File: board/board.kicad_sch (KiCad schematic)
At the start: 22 parts, among them J1 UART, J2 008_USB, J3 DebugEdge_02x05, J4 SPI_2x3, J5 ADC_2x3, J6 I2C_2x2, J7 SPI_2x3, J8 I2C_2x2, J9 UART_2x2

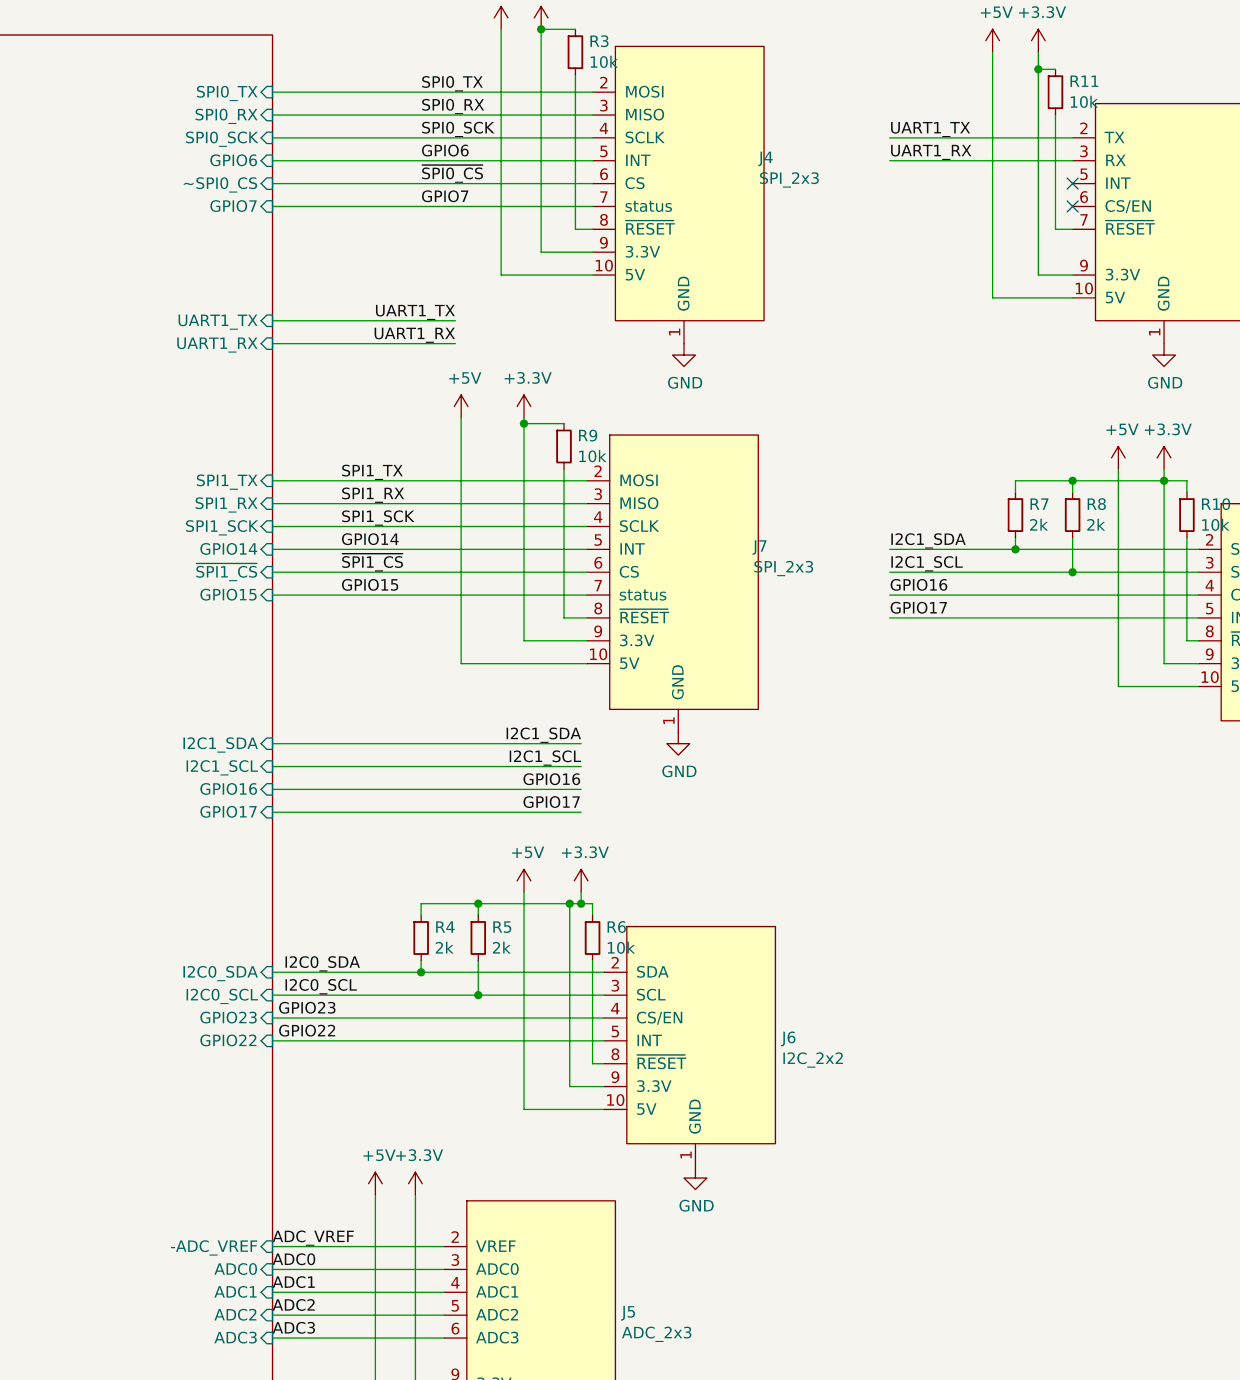
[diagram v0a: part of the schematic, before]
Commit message: changed top I2C connector to be a UNIO connector for a mac address chip
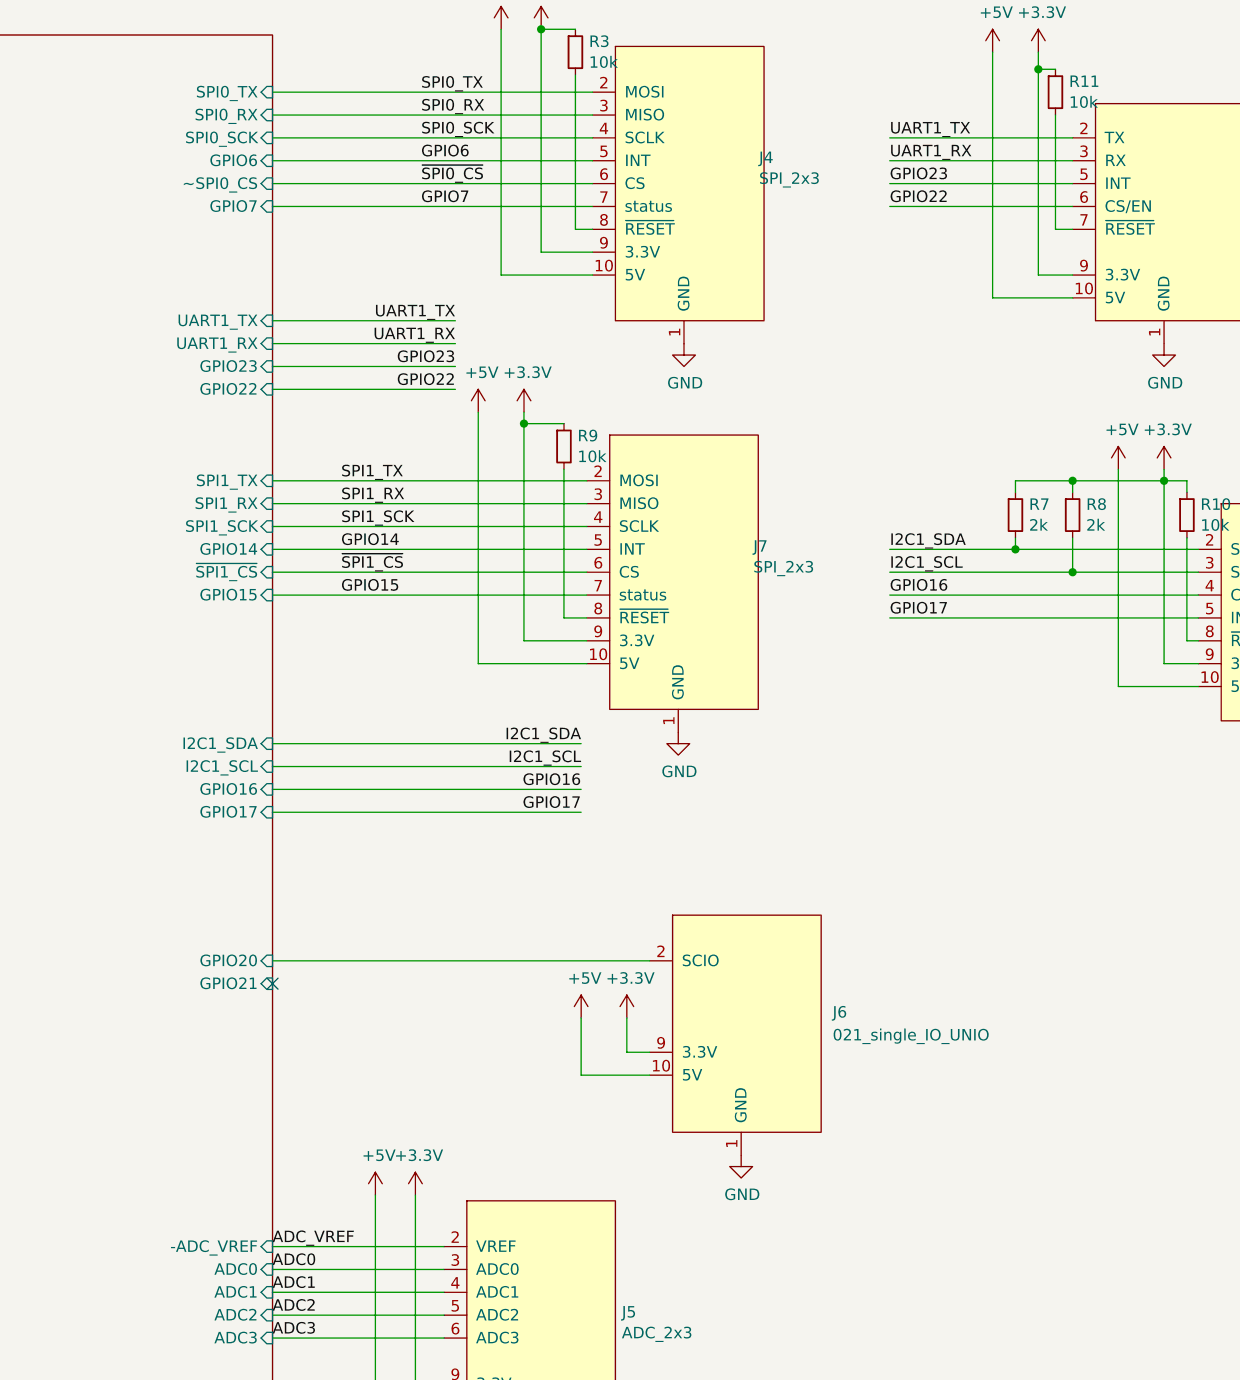
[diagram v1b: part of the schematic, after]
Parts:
- removed J6: I2C_2x2, on_edge:on_edge_2x05_up_host, symbol put_on_edge:001_I2C
- removed R4, R5: 2k, Resistor_SMD:R_0603_1608Metric, symbol Device:R_Small
- removed R6: 10k, Resistor_SMD:R_0603_1608Metric, symbol Device:R_Small
- added J6: 021_single_IO_UNIO, on_edge:on_edge_2x05_up_host, symbol put_on_edge:021_single_IO_UNIO
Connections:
- net +3V3: now also J6.9 (3.3V)
- net +5V: now also J6.10 (5V)
- net GND: now also J6.1 (GND)
- net GPIO22: now also J9.6 (CS/EN)
- net GPIO23: now also J9.5 (INT)
- new net rp2040/GPIO20: J6.2 (SCIO)
- no-connect marks 12 -> 11
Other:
- sheet rp2040 ports: added GPIO20, GPIO21; removed I2C0_SCL, I2C0_SDA

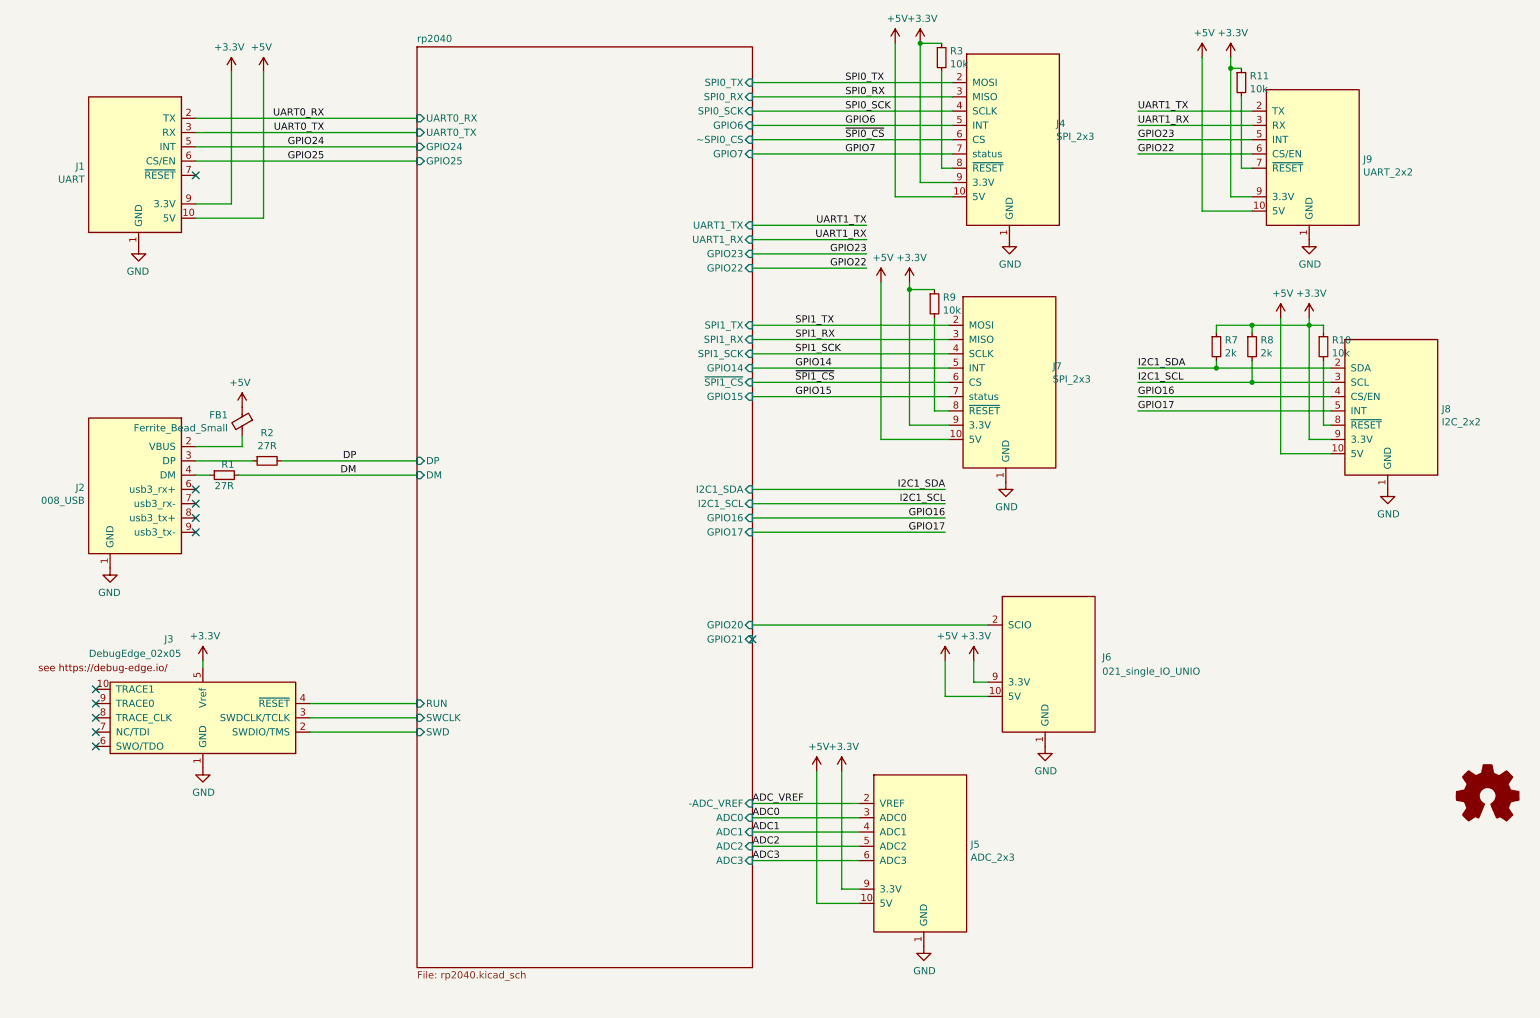
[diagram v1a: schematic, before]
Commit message: changed power symbols in subsheets
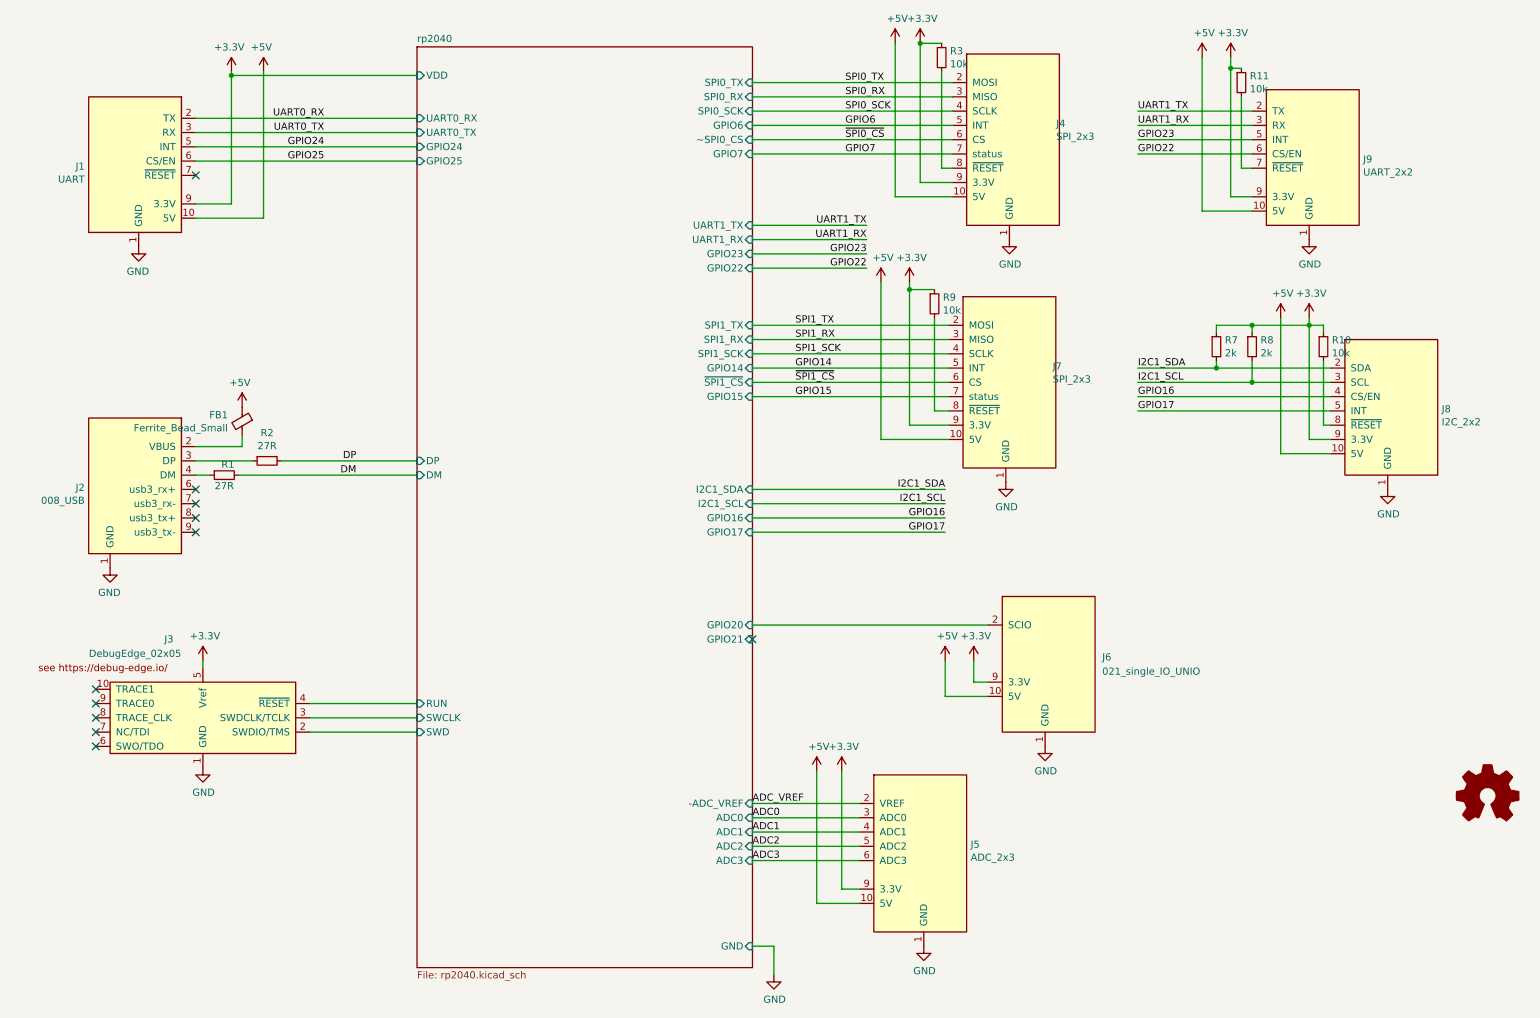
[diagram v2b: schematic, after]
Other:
- sheet rp2040 ports: added GND, VDD; removed none
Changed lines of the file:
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@@
   (junction (at 241.3 69.85) (diameter 0) (color 0 0 0 0)
+  )
+  (junction (at 49.53 25.4) (diameter 0) (color 0 0 0 0)
   )
   (junction (at 172.085 19.685) (diameter 0) (color 0 0 0 0)
@@
     (stroke (width 0) (type default) (color 0 0 0 0))
   )
+  (wire (pts (xy 146.05 180.34) (xy 142.24 180.34))
+    (stroke (width 0) (type default) (color 0 0 0 0))
+  )
   (wire (pts (xy 241.3 90.17) (xy 245.11 90.17))
     (stroke (width 0) (type default) (color 0 0 0 0))
@@
     (stroke (width 0) (type default) (color 0 0 0 0))
   )
-  (wire (pts (xy 49.53 24.765) (xy 49.53 48.26))
+  (wire (pts (xy 49.53 24.765) (xy 49.53 25.4))
     (stroke (width 0) (type default) (color 0 0 0 0))
   )
@@
     (stroke (width 0) (type default) (color 0 0 0 0))
   )
+  (wire (pts (xy 49.53 25.4) (xy 82.55 25.4))
+    (stroke (width 0) (type default) (color 0 0 0 0))
+  )
   (wire (pts (xy 243.84 69.85) (xy 243.84 71.12))
     (stroke (width 0) (type default) (color 0 0 0 0))
@@
     (stroke (width 0) (type default) (color 0 0 0 0))
   )
+  (wire (pts (xy 146.05 185.42) (xy 146.05 180.34))
+    (stroke (width 0) (type default) (color 0 0 0 0))
+  )
   (wire (pts (xy 222.25 49.53) (xy 231.14 49.53))
     (stroke (width 0) (type default) (color 0 0 0 0))
   )
   (wire (pts (xy 172.085 19.685) (xy 172.085 44.45))
+    (stroke (width 0) (type default) (color 0 0 0 0))
+  )
+  (wire (pts (xy 49.53 25.4) (xy 49.53 48.26))
     (stroke (width 0) (type default) (color 0 0 0 0))
   )
@@
     (pin "1")
   )
+  (symbol (lib_id "power:GND") (at 146.05 185.42 0) (unit 1)
+    (in_bom yes) (on_board yes)
+    (property "Reference" "#PWR?" (id 0) (at 146.05 191.77 0)
+      (effects (font (size 1.27 1.27)) hide)
+    )
+    (property "Value" "GND" (id 1) (at 146.177 189.8142 0))
+    (property "Footprint" "" (id 2) (at 146.05 185.42 0)
+      (effects (font (size 1.27 1.27)) hide)
+    )
+    (property "Datasheet" "" (id 3) (at 146.05 185.42 0)
+      (effects (font (size 1.27 1.27)) hide)
+    )
+    (pin "1")
+  )
   (symbol (lib_id "power:+5V") (at 153.67 149.225 0) (unit 1)
     (in_bom yes) (on_board yes)
@@
       (effects (font (size 1.27 1.27)) (justify right))
     )
+    (pin "GND" input (at 142.24 180.34 0)
+      (effects (font (size 1.27 1.27)) (justify right))
+    )
+    (pin "VDD" input (at 82.55 25.4 180)
+      (effects (font (size 1.27 1.27)) (justify left))
+    )
   )
   (sheet_instances
@@
       (reference "#PWR0125") (unit 1) (value "GND") (footprint "")
     )
-    (path "/767ce4c6-0e55-4543-92f0-34cb8237a544/552dce0a-dd62-4b75-bb84-8f635cf1301d"
-      (reference "#PWR0126") (unit 1) (value "GND") (footprint "")
-    )
-    (path "/767ce4c6-0e55-4543-92f0-34cb8237a544/dfb74bbc-61c1-495a-ad7b-f4ebbd9c0010"
-      (reference "#PWR0127") (unit 1) (value "GND") (footprint "")
-    )
-    (path "/767ce4c6-0e55-4543-92f0-34cb8237a544/8dc4ebfc-0e77-40ed-9afb-b833d7007905"
-      (reference "#PWR0128") (unit 1) (value "GND") (footprint "")
-    )
-    (path "/767ce4c6-0e55-4543-92f0-34cb8237a544/dfa49b32-8959-4a81-98ca-3a032bed62d5"
-      (reference "#PWR0129") (unit 1) (value "GND") (footprint "")
-    )
-    (path "/767ce4c6-0e55-4543-92f0-34cb8237a544/782e37df-d3a5-4165-85f3-e14f913b989f"
-      (reference "#PWR0130") (unit 1) (value "GND") (footprint "")
-    )
-    (path "/767ce4c6-0e55-4543-92f0-34cb8237a544/88f52a24-2203-4546-90ee-0cd55bd0cd35"
-      (reference "#PWR0131") (unit 1) (value "+3.3V") (footprint "")
-    )
-    (path "/767ce4c6-0e55-4543-92f0-34cb8237a544/8b1628b6-a8d8-4248-a69a-7b664bbb34e1"
-      (reference "#PWR0132") (unit 1) (value "GND") (footprint "")
-    )
-    (path "/767ce4c6-0e55-4543-92f0-34cb8237a544/ab0a00b3-5e4c-489c-80bf-e28962852f41"
-      (reference "#PWR0133") (unit 1) (value "GND") (footprint "")
-    )
-    (path "/767ce4c6-0e55-4543-92f0-34cb8237a544/7f18e575-6c18-46d1-aafd-24358927dbd8"
-      (reference "#PWR0134") (unit 1) (value "GND") (footprint "")
-    )
-    (path "/767ce4c6-0e55-4543-92f0-34cb8237a544/a81f50a3-a9e0-4cab-b7c7-d0df444e6988"
-      (reference "#PWR0135") (unit 1) (value "+3.3V") (footprint "")
-    )
-    (path "/767ce4c6-0e55-4543-92f0-34cb8237a544/b6d1f93d-18c5-4247-a972-8cc2bc717483"
-      (reference "#PWR0136") (unit 1) (value "+3.3V") (footprint "")
-    )
-    (path "/767ce4c6-0e55-4543-92f0-34cb8237a544/7d2cd37f-4022-4193-8ef4-41c965ce3b84"
-      (reference "#PWR0137") (unit 1) (value "+3.3V") (footprint "")
-    )
-    (path "/767ce4c6-0e55-4543-92f0-34cb8237a544/b963ddb8-2875-4680-933b-203e75329d55"
-      (reference "#PWR0138") (unit 1) (value "GND") (footprint "")
-    )
-    (path "/767ce4c6-0e55-4543-92f0-34cb8237a544/eabfe023-aec3-483f-8b1d-912270f4a596"
-      (reference "#PWR0139") (unit 1) (value "GND") (footprint "")
-    )
-    (path "/767ce4c6-0e55-4543-92f0-34cb8237a544/94c558b8-6551-4f3b-8e99-37d025298c68"
-      (reference "#PWR0140") (unit 1) (value "GND") (footprint "")
-    )
-    (path "/767ce4c6-0e55-4543-92f0-34cb8237a544/f26a52dd-695a-4dc4-bcd8-5fa404a8e0ab"
-      (reference "#PWR0141") (unit 1) (value "GND") (footprint "")
-    )
-    (path "/767ce4c6-0e55-4543-92f0-34cb8237a544/c9d8f090-5d6b-4e11-a958-24cdf3511aa9"
-      (reference "#PWR0142") (unit 1) (value "GND") (footprint "")
-    )
-    (path "/767ce4c6-0e55-4543-92f0-34cb8237a544/fb95128d-f0c0-449b-ad58-e8c2b1cba2dc"
-      (reference "#PWR0143") (unit 1) (value "+3.3V") (footprint "")
-    )
-    (path "/767ce4c6-0e55-4543-92f0-34cb8237a544/3b268ad6-2c2e-4cd7-8af2-09452ea40aa8"
-      (reference "#PWR0144") (unit 1) (value "+3.3V") (footprint "")
-    )
-    (path "/767ce4c6-0e55-4543-92f0-34cb8237a544/7ca933af-87da-421b-b030-b81e7722a72b"
-      (reference "#PWR0145") (unit 1) (value "+3.3V") (footprint "")
-    )
-    (path "/767ce4c6-0e55-4543-92f0-34cb8237a544/7b3c5e0d-89c7-4a38-aa4c-09cf8e184831"
-      (reference "#PWR0146") (unit 1) (value "GND") (footprint "")
-    )
-    (path "/767ce4c6-0e55-4543-92f0-34cb8237a544/cb1d7b7c-80f2-46a6-84bb-7debf3df06ab"
-      (reference "#PWR0147") (unit 1) (value "GND") (footprint "")
-    )
-    (path "/767ce4c6-0e55-4543-92f0-34cb8237a544/2d5e37cb-a2ab-4022-a5ea-16b85f604442"
-      (reference "#PWR0148") (unit 1) (value "+3.3V") (footprint "")
-    )
-    (path "/767ce4c6-0e55-4543-92f0-34cb8237a544/6c6d92f9-5833-4cdc-8d1b-4fcd5186a0c7"
-      (reference "#PWR0149") (unit 1) (value "+3.3V") (footprint "")
-    )
-    (path "/767ce4c6-0e55-4543-92f0-34cb8237a544/5439881e-7cc4-4597-80b0-ddfacdcf9478"
-      (reference "#PWR0150") (unit 1) (value "+3.3V") (footprint "")
-    )
-    (path "/767ce4c6-0e55-4543-92f0-34cb8237a544/3dab29f0-5e56-4a74-b163-e861c805a04b"
-      (reference "#PWR0151") (unit 1) (value "GND") (footprint "")
-    )
-    (path "/767ce4c6-0e55-4543-92f0-34cb8237a544/1a31f670-54d2-42e2-bd8b-3e2be53be507"
-      (reference "#PWR0152") (unit 1) (value "+3.3V") (footprint "")
-    )
-    (path "/767ce4c6-0e55-4543-92f0-34cb8237a544/22f6936f-2174-4bdf-a9e8-a8eb887c4f22"
-      (reference "#PWR0153") (unit 1) (value "GND") (footprint "")
-    )
-    (path "/767ce4c6-0e55-4543-92f0-34cb8237a544/efabbb76-38c7-48c5-a530-e95e3297d550"
-      (reference "#PWR0154") (unit 1) (value "+3.3V") (footprint "")
-    )
-    (path "/767ce4c6-0e55-4543-92f0-34cb8237a544/4dc0b55c-ed9c-4744-b7c5-6455cd53c86e"
-      (reference "#PWR0155") (unit 1) (value "GND") (footprint "")
+    (path "/bc3a5d7d-4393-4a0f-9f60-20b79bdb544d"
+      (reference "#PWR?") (unit 1) (value "GND") (footprint "")
     )
     (path "/767ce4c6-0e55-4543-92f0-34cb8237a544/ce35c40f-cc2d-44ae-a1e7-c961ca76d76a"
@@
       (reference "C14") (unit 1) (value "2.2uF") (footprint "Capacitor_SMD:C_0603_1608Metric")
     )
+    (path "/767ce4c6-0e55-4543-92f0-34cb8237a544/006b1f66-b929-4026-b35d-2311bff51e83"
+      (reference "C29") (unit 1) (value "100nF") (footprint "Capacitor_SMD:C_0603_1608Metric")
+    )
     (path "/cc887ae8-b7ce-4987-bf3f-2cbf78a0be76"
